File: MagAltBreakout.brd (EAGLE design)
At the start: 49.5 x 22.9 mm, 0 parts

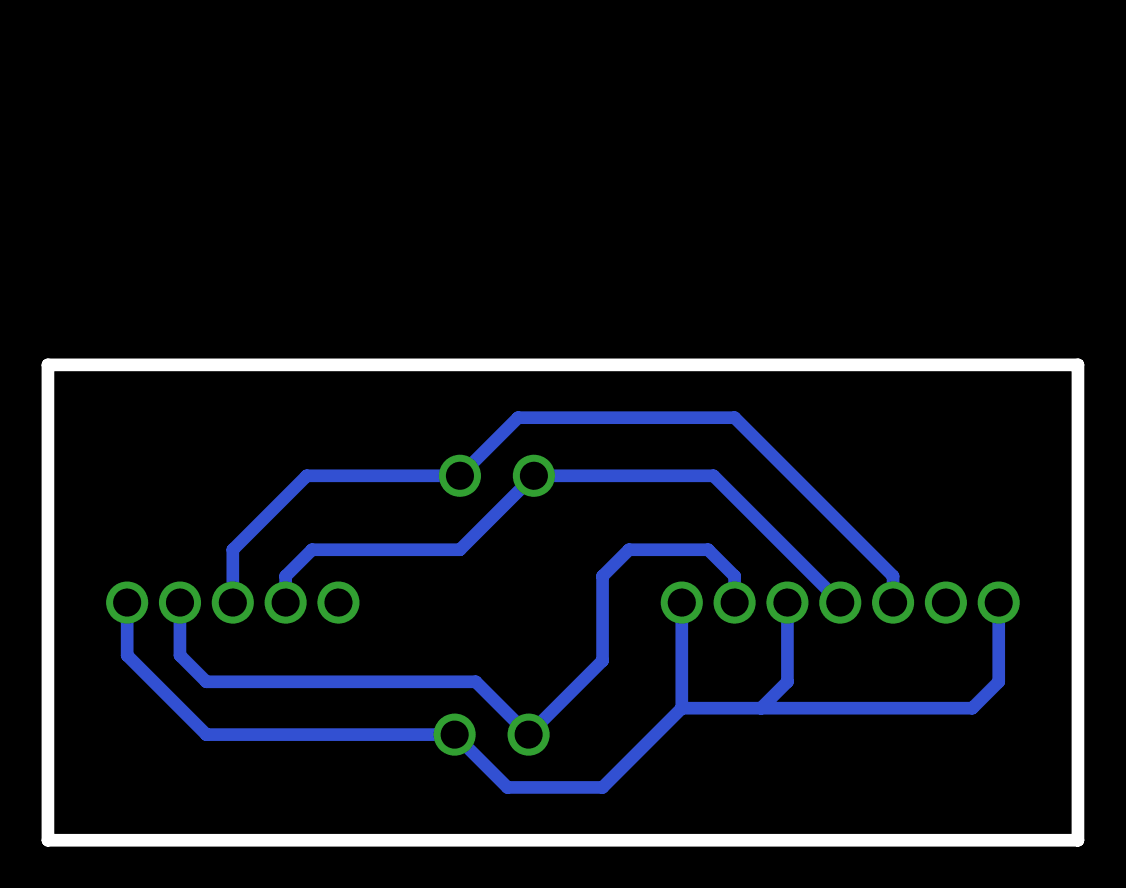
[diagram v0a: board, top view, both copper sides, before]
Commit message: Fixed Altimeter PS pin connection on breakout board (was connected to GND, now connected to VCC)
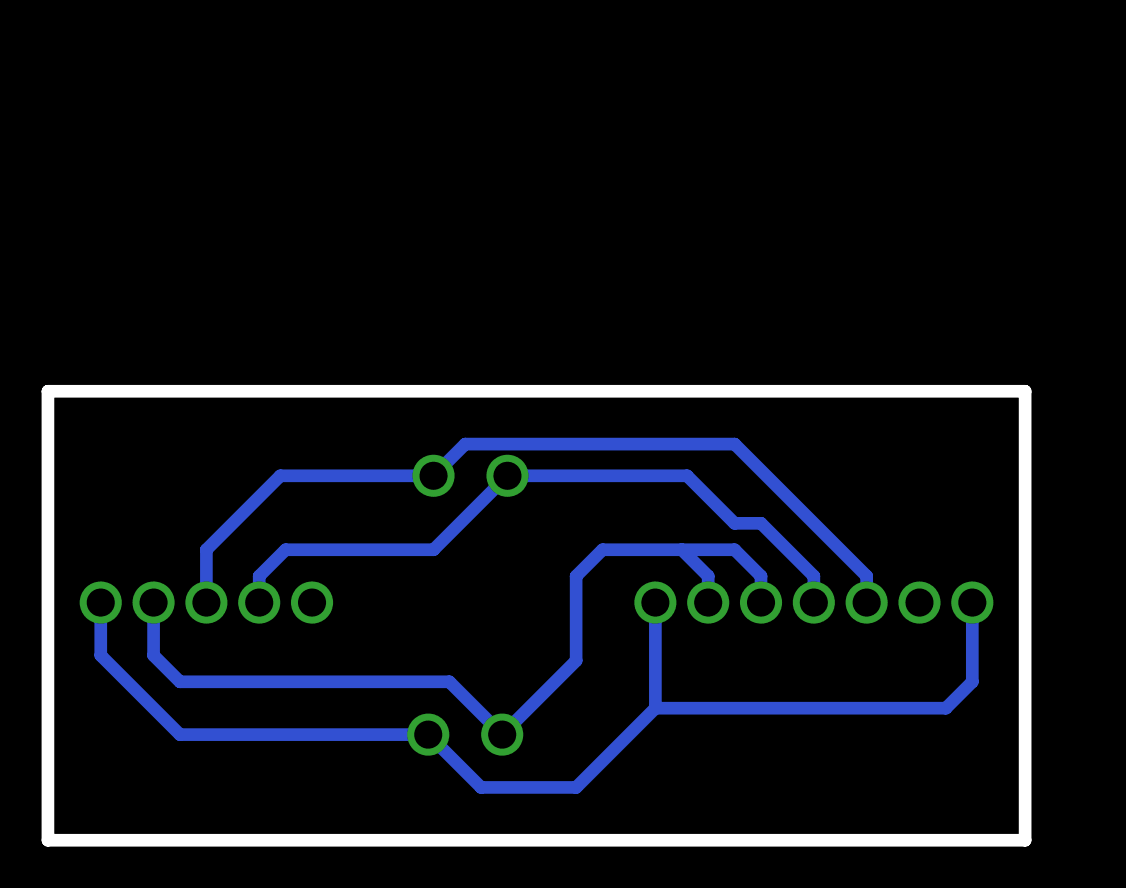
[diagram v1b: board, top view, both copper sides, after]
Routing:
- net VCC: track 38.6 -> 44.3 mm, vias 3 -> 4
- net GND: track 63.7 -> 58.1 mm, vias 5 -> 4
- net SDA: track 41.3 -> 40.3 mm
- net SCL: track 32.5 -> 33.2 mm
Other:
- board size 49.5 x 22.9 mm -> 47 x 21.6 mm
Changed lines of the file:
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@@
 <plain>
 <polygon width="0.6096" layer="20">
-<vertex x="49.53" y="22.86"/>
-<vertex x="49.53" y="0"/>
+<vertex x="46.99" y="21.59"/>
+<vertex x="46.99" y="0"/>
 <vertex x="0" y="0"/>
-<vertex x="0" y="22.86"/>
+<vertex x="0" y="21.59"/>
 </polygon>
 </plain>
@@
 <signals>
 <signal name="VCC">
-<via x="6.35" y="11.43" extent="1-16" drill="1.35"/>
-<via x="33.02" y="11.43" extent="1-16" drill="1.35"/>
-<via x="23.114" y="5.08" extent="1-16" drill="1.35"/>
-<wire x1="23.114" y1="5.08" x2="20.574" y2="7.62" width="0.6096" layer="16"/>
-<wire x1="20.574" y1="7.62" x2="7.62" y2="7.62" width="0.6096" layer="16"/>
-<wire x1="7.62" y1="7.62" x2="6.35" y2="8.89" width="0.6096" layer="16"/>
-<wire x1="6.35" y1="8.89" x2="6.35" y2="11.43" width="0.6096" layer="16"/>
-<wire x1="23.114" y1="5.08" x2="26.67" y2="8.636" width="0.6096" layer="16"/>
-<wire x1="26.67" y1="8.636" x2="26.67" y2="12.7" width="0.6096" layer="16"/>
-<wire x1="26.67" y1="12.7" x2="27.94" y2="13.97" width="0.6096" layer="16"/>
-<wire x1="27.94" y1="13.97" x2="31.75" y2="13.97" width="0.6096" layer="16"/>
-<wire x1="31.75" y1="13.97" x2="33.02" y2="12.7" width="0.6096" layer="16"/>
-<wire x1="33.02" y1="12.7" x2="33.02" y2="11.43" width="0.6096" layer="16"/>
+<via x="5.08" y="11.43" extent="1-16" drill="1.35"/>
+<via x="31.75" y="11.43" extent="1-16" drill="1.35"/>
+<via x="21.844" y="5.08" extent="1-16" drill="1.35"/>
+<wire x1="21.844" y1="5.08" x2="19.304" y2="7.62" width="0.6096" layer="16"/>
+<wire x1="19.304" y1="7.62" x2="6.35" y2="7.62" width="0.6096" layer="16"/>
+<wire x1="6.35" y1="7.62" x2="5.08" y2="8.89" width="0.6096" layer="16"/>
+<wire x1="5.08" y1="8.89" x2="5.08" y2="11.43" width="0.6096" layer="16"/>
+<wire x1="21.844" y1="5.08" x2="25.4" y2="8.636" width="0.6096" layer="16"/>
+<wire x1="25.4" y1="8.636" x2="25.4" y2="12.7" width="0.6096" layer="16"/>
+<wire x1="25.4" y1="12.7" x2="26.67" y2="13.97" width="0.6096" layer="16"/>
+<wire x1="26.67" y1="13.97" x2="30.48" y2="13.97" width="0.6096" layer="16"/>
+<wire x1="30.48" y1="13.97" x2="31.75" y2="12.7" width="0.6096" layer="16"/>
+<wire x1="31.75" y1="12.7" x2="31.75" y2="11.43" width="0.6096" layer="16"/>
+<via x="34.29" y="11.43" extent="1-16" drill="1.35"/>
+<wire x1="30.48" y1="13.97" x2="33.02" y2="13.97" width="0.6096" layer="16"/>
+<wire x1="33.02" y1="13.97" x2="34.29" y2="12.7" width="0.6096" layer="16"/>
+<wire x1="34.29" y1="12.7" x2="34.29" y2="11.43" width="0.6096" layer="16"/>
 </signal>
 <signal name="SDA">
-<via x="8.89" y="11.43" extent="1-16" drill="1.35"/>
-<via x="40.64" y="11.43" extent="1-16" drill="1.35"/>
-<via x="19.812" y="17.526" extent="1-16" drill="1.35"/>
-<wire x1="19.812" y1="17.526" x2="12.446" y2="17.526" width="0.6096" layer="16"/>
-<wire x1="12.446" y1="17.526" x2="8.89" y2="13.97" width="0.6096" layer="16"/>
-<wire x1="8.89" y1="13.97" x2="8.89" y2="11.43" width="0.6096" layer="16"/>
-<wire x1="19.812003125" y1="17.526003125" x2="22.605996875" y2="20.319996875" width="0.6096" layer="16"/>
-<wire x1="22.605996875" y1="20.319996875" x2="33.02" y2="20.32" width="0.6096" layer="16"/>
-<wire x1="33.02" y1="20.32" x2="40.64" y2="12.7" width="0.6096" layer="16"/>
-<wire x1="40.64" y1="12.7" x2="40.64" y2="11.43" width="0.6096" layer="16"/>
+<via x="7.62" y="11.43" extent="1-16" drill="1.35"/>
+<via x="39.37" y="11.43" extent="1-16" drill="1.35"/>
+<via x="18.542" y="17.526" extent="1-16" drill="1.35"/>
+<wire x1="18.542" y1="17.526" x2="11.176" y2="17.526" width="0.6096" layer="16"/>
+<wire x1="11.176" y1="17.526" x2="7.62" y2="13.97" width="0.6096" layer="16"/>
+<wire x1="7.62" y1="13.97" x2="7.62" y2="11.43" width="0.6096" layer="16"/>
+<wire x1="39.37" y1="12.7" x2="39.37" y2="11.43" width="0.6096" layer="16"/>
+<wire x1="18.542" y1="17.526" x2="20.066" y2="19.05" width="0.6096" layer="16"/>
+<wire x1="20.066" y1="19.05" x2="33.02" y2="19.05" width="0.6096" layer="16"/>
+<wire x1="33.02" y1="19.05" x2="39.37" y2="12.7" width="0.6096" layer="16"/>
 </signal>
 <signal name="SCL">
-<via x="11.43" y="11.43" extent="1-16" drill="1.35"/>
-<via x="38.1" y="11.43" extent="1-16" drill="1.35"/>
-<via x="23.368" y="17.526" extent="1-16" drill="1.35"/>
-<wire x1="23.368" y1="17.526" x2="32.004" y2="17.526" width="0.6096" layer="16"/>
-<wire x1="32.004" y1="17.526" x2="38.1" y2="11.43" width="0.6096" layer="16"/>
-<wire x1="23.368" y1="17.526" x2="19.812" y2="13.97" width="0.6096" layer="16"/>
-<wire x1="19.812" y1="13.97" x2="12.7" y2="13.97" width="0.6096" layer="16"/>
-<wire x1="12.7" y1="13.97" x2="11.43" y2="12.7" width="0.6096" layer="16"/>
-<wire x1="11.43" y1="12.7" x2="11.43" y2="11.43" width="0.6096" layer="16"/>
+<via x="10.16" y="11.43" extent="1-16" drill="1.35"/>
+<via x="36.83" y="11.43" extent="1-16" drill="1.35"/>
+<via x="22.098" y="17.526" extent="1-16" drill="1.35"/>
+<wire x1="22.098" y1="17.526" x2="30.734" y2="17.526" width="0.6096" layer="16"/>
+<wire x1="22.098" y1="17.526" x2="18.542" y2="13.97" width="0.6096" layer="16"/>
+<wire x1="18.542" y1="13.97" x2="11.43" y2="13.97" width="0.6096" layer="16"/>
+<wire x1="11.43" y1="13.97" x2="10.16" y2="12.7" width="0.6096" layer="16"/>
+<wire x1="10.16" y1="12.7" x2="10.16" y2="11.43" width="0.6096" layer="16"/>
+<wire x1="30.734" y1="17.526" x2="33.02" y2="15.24" width="0.6096" layer="16"/>
+<wire x1="33.02" y1="15.24" x2="34.29" y2="15.24" width="0.6096" layer="16"/>
+<wire x1="34.29" y1="15.24" x2="36.83" y2="12.7" width="0.6096" layer="16"/>
+<wire x1="36.83" y1="12.7" x2="36.83" y2="11.43" width="0.6096" layer="16"/>
 </signal>
 <signal name="GND">
-<via x="3.81" y="11.43" extent="1-16" drill="1.35"/>
-<via x="30.48" y="11.43" extent="1-16" drill="1.35"/>
-<via x="35.56" y="11.43" extent="1-16" drill="1.35"/>
-<via x="45.72" y="11.43" extent="1-16" drill="1.35"/>
-<via x="19.558" y="5.08" extent="1-16" drill="1.35"/>
-<wire x1="19.558" y1="5.08" x2="7.62" y2="5.08" width="0.6096" layer="16"/>
-<wire x1="7.62" y1="5.08" x2="3.81" y2="8.89" width="0.6096" layer="16"/>
-<wire x1="3.81" y1="8.89" x2="3.81" y2="11.43" width="0.6096" layer="16"/>
-<wire x1="19.558" y1="5.08" x2="22.098" y2="2.54" width="0.6096" layer="16"/>
-<wire x1="26.67" y1="2.54" x2="30.48" y2="6.35" width="0.6096" layer="16"/>
-<wire x1="30.48" y1="6.35" x2="30.48" y2="11.43" width="0.6096" layer="16"/>
-<wire x1="22.098" y1="2.54" x2="26.67" y2="2.54" width="0.6096" layer="16"/>
-<wire x1="30.48" y1="6.35" x2="34.29" y2="6.35" width="0.6096" layer="16"/>
-<wire x1="34.29" y1="6.35" x2="35.56" y2="7.62" width="0.6096" layer="16"/>
-<wire x1="35.56" y1="7.62" x2="35.56" y2="11.43" width="0.6096" layer="16"/>
-<wire x1="34.29" y1="6.35" x2="44.45" y2="6.35" width="0.6096" layer="16"/>
-<wire x1="44.45" y1="6.35" x2="45.72" y2="7.62" width="0.6096" layer="16"/>
-<wire x1="45.72" y1="7.62" x2="45.72" y2="11.43" width="0.6096" layer="16"/>
+<via x="2.54" y="11.43" extent="1-16" drill="1.35"/>
+<via x="29.21" y="11.43" extent="1-16" drill="1.35"/>
+<via x="44.45" y="11.43" extent="1-16" drill="1.35"/>
+<via x="18.288" y="5.08" extent="1-16" drill="1.35"/>
+<wire x1="18.288" y1="5.08" x2="6.35" y2="5.08" width="0.6096" layer="16"/>
+<wire x1="6.35" y1="5.08" x2="2.54" y2="8.89" width="0.6096" layer="16"/>
+<wire x1="2.54" y1="8.89" x2="2.54" y2="11.43" width="0.6096" layer="16"/>
+<wire x1="18.288" y1="5.08" x2="20.828" y2="2.54" width="0.6096" layer="16"/>
+<wire x1="25.4" y1="2.54" x2="29.21" y2="6.35" width="0.6096" layer="16"/>
+<wire x1="29.21" y1="6.35" x2="29.21" y2="11.43" width="0.6096" layer="16"/>
+<wire x1="20.828" y1="2.54" x2="25.4" y2="2.54" width="0.6096" layer="16"/>
+<wire x1="29.21" y1="6.35" x2="43.18" y2="6.35" width="0.6096" layer="16"/>
+<wire x1="43.18" y1="6.35" x2="44.45" y2="7.62" width="0.6096" layer="16"/>
+<wire x1="44.45" y1="7.62" x2="44.45" y2="11.43" width="0.6096" layer="16"/>
 </signal>
 <signal name="INT">
-<via x="13.97" y="11.43" extent="1-16" drill="1.35"/>
+<via x="12.7" y="11.43" extent="1-16" drill="1.35"/>
 </signal>
 <signal name="C6">
-<via x="43.18" y="11.43" extent="1-16" drill="1.35"/>
+<via x="41.91" y="11.43" extent="1-16" drill="1.35"/>
 </signal>
 </signals>

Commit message: Made breakout board more aesthetic
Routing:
- net VCC: track 44.3 -> 45.6 mm
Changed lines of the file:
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@@
 <via x="31.75" y="11.43" extent="1-16" drill="1.35"/>
 <via x="21.844" y="5.08" extent="1-16" drill="1.35"/>
-<wire x1="21.844" y1="5.08" x2="19.304" y2="7.62" width="0.6096" layer="16"/>
-<wire x1="19.304" y1="7.62" x2="6.35" y2="7.62" width="0.6096" layer="16"/>
-<wire x1="6.35" y1="7.62" x2="5.08" y2="8.89" width="0.6096" layer="16"/>
+<wire x1="5.08" y1="8.89" x2="6.35" y2="7.62" width="0.6096" layer="16"/>
 <wire x1="5.08" y1="8.89" x2="5.08" y2="11.43" width="0.6096" layer="16"/>
-<wire x1="21.844" y1="5.08" x2="25.4" y2="8.636" width="0.6096" layer="16"/>
-<wire x1="25.4" y1="8.636" x2="25.4" y2="12.7" width="0.6096" layer="16"/>
+<wire x1="25.4" y1="8.89" x2="25.4" y2="12.7" width="0.6096" layer="16"/>
 <wire x1="25.4" y1="12.7" x2="26.67" y2="13.97" width="0.6096" layer="16"/>
 <wire x1="26.67" y1="13.97" x2="30.48" y2="13.97" width="0.6096" layer="16"/>
@@
 <wire x1="33.02" y1="13.97" x2="34.29" y2="12.7" width="0.6096" layer="16"/>
 <wire x1="34.29" y1="12.7" x2="34.29" y2="11.43" width="0.6096" layer="16"/>
+<wire x1="24.13" y1="7.62" x2="25.4" y2="8.89" width="0.6096" layer="16"/>
+<wire x1="6.35" y1="7.62" x2="19.304" y2="7.62" width="0.6096" layer="16"/>
+<wire x1="19.304" y1="7.62" x2="24.13" y2="7.62" width="0.6096" layer="16"/>
+<wire x1="21.844" y1="5.08" x2="19.304" y2="7.62" width="0.6096" layer="16"/>
 </signal>
 <signal name="SDA">
@@
 <wire x1="2.54" y1="8.89" x2="2.54" y2="11.43" width="0.6096" layer="16"/>
 <wire x1="18.288" y1="5.08" x2="20.828" y2="2.54" width="0.6096" layer="16"/>
-<wire x1="25.4" y1="2.54" x2="29.21" y2="6.35" width="0.6096" layer="16"/>
-<wire x1="29.21" y1="6.35" x2="29.21" y2="11.43" width="0.6096" layer="16"/>
-<wire x1="20.828" y1="2.54" x2="25.4" y2="2.54" width="0.6096" layer="16"/>
-<wire x1="29.21" y1="6.35" x2="43.18" y2="6.35" width="0.6096" layer="16"/>
+<wire x1="20.828" y1="2.54" x2="24.13" y2="2.54" width="0.6096" layer="16"/>
 <wire x1="43.18" y1="6.35" x2="44.45" y2="7.62" width="0.6096" layer="16"/>
 <wire x1="44.45" y1="7.62" x2="44.45" y2="11.43" width="0.6096" layer="16"/>
+<wire x1="29.21" y1="7.62" x2="29.21" y2="11.43" width="0.6096" layer="16"/>
+<wire x1="24.13" y1="2.54" x2="29.21" y2="7.62" width="0.6096" layer="16"/>
+<wire x1="29.21" y1="7.62" x2="30.48" y2="6.35" width="0.6096" layer="16"/>
+<wire x1="30.48" y1="6.35" x2="43.18" y2="6.35" width="0.6096" layer="16"/>
 </signal>
 <signal name="INT">

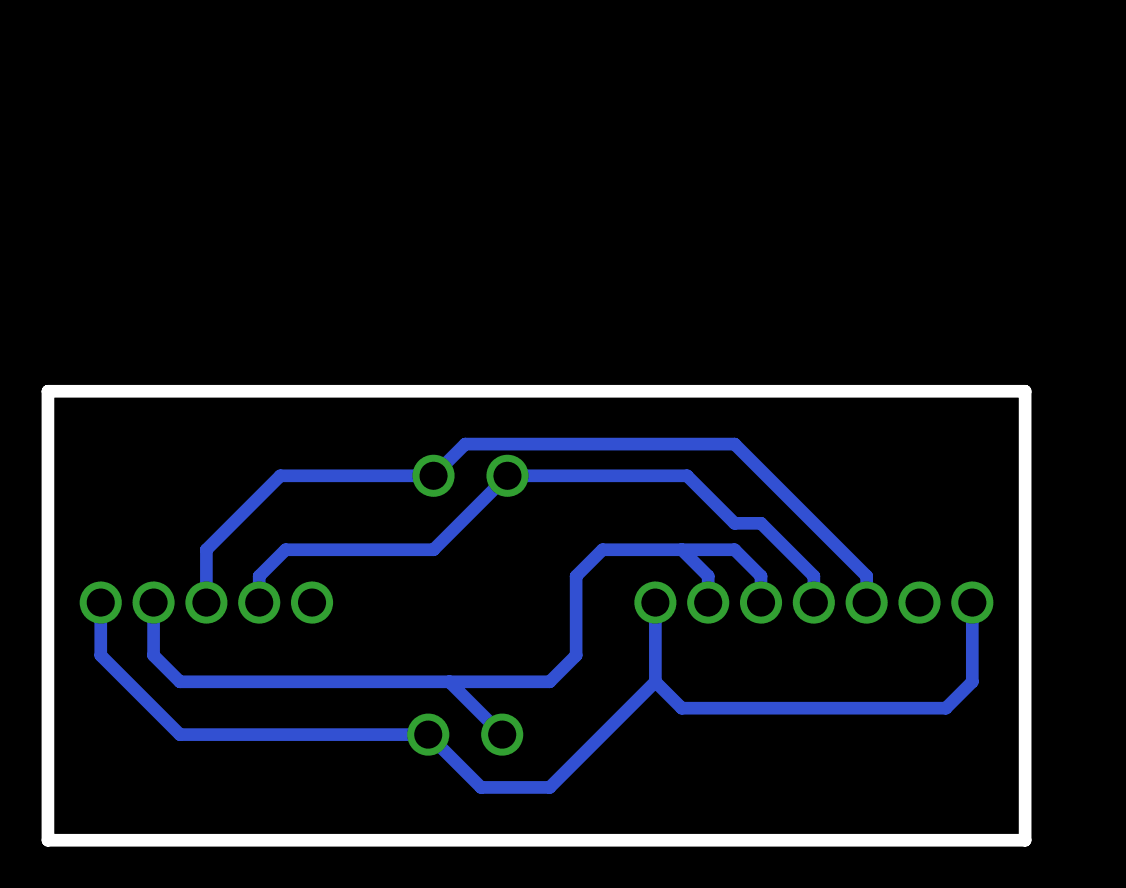
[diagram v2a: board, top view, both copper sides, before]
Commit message: Made both breakout boards REALLY aesthetic, also they self document now
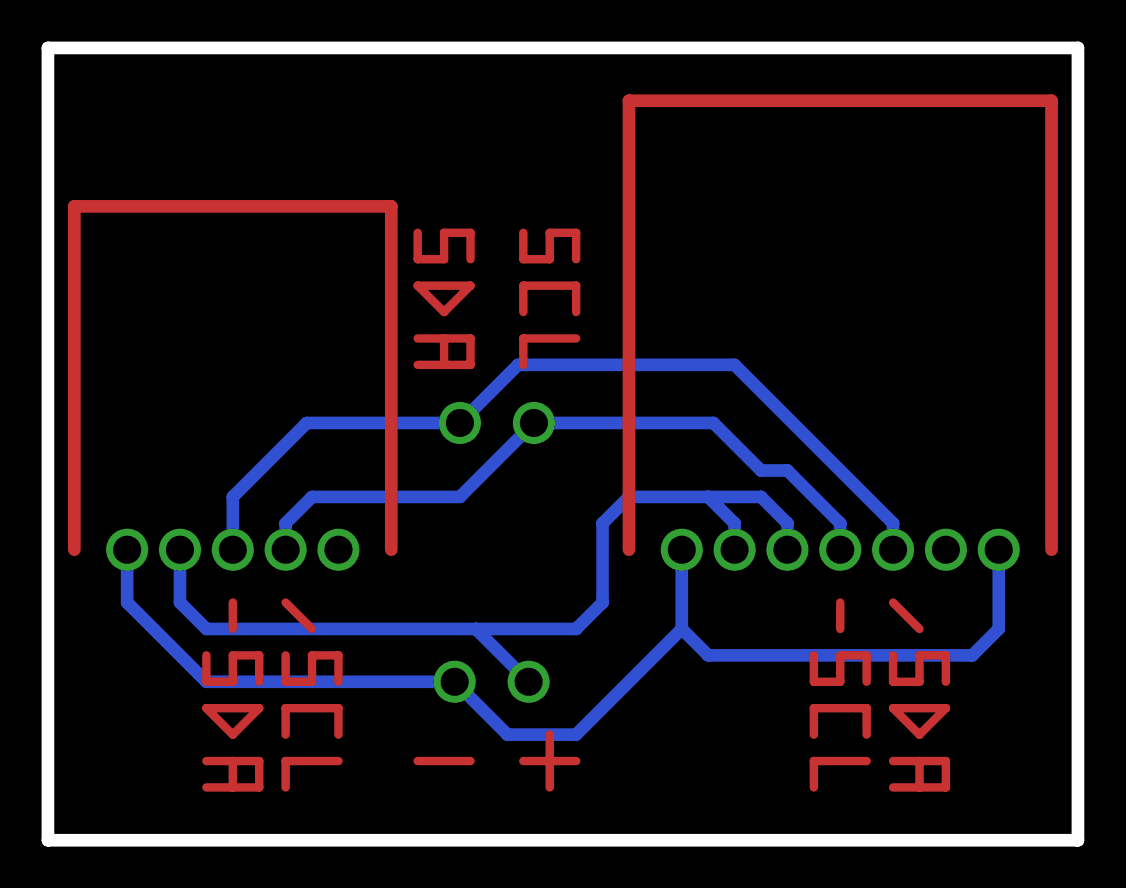
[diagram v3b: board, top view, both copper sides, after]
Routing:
- net S$1: track 0.00 -> 63.5 mm
- net S$2: track 0.00 -> 48.3 mm
- net S$15: track 0.00 -> 7.62 mm
- net S$3: track 0.00 -> 7.62 mm
- net S$26: track 0.00 -> 7.62 mm
- net S$16: track 0.00 -> 6.35 mm
- net S$12: track 0.00 -> 6.35 mm
- net S$24: track 0.00 -> 6.35 mm
- net S$21: track 0.00 -> 6.35 mm
- net S$6: track 0.00 -> 6.35 mm
- net S$5: track 0.00 -> 6.35 mm
- net S$4: track 0.00 -> 6.13 mm
- net S$13: track 0.00 -> 6.13 mm
- net S$25: track 0.00 -> 6.13 mm
- net S$7: track 0.00 -> 5.08 mm
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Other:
- board size 47 x 21.6 mm -> 49.5 x 38.1 mm
